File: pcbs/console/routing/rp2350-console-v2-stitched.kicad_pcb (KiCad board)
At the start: 4 copper layers, 72 x 66 mm, 81 parts, among them J1 TYPE-C-31-M-12, J2 HDMI-001S, J3 B10B-XH-A(LF)(SN), J4 B10B-XH-A(LF)(SN), J5 B2B-PH-K-S(LF)(SN), U1 SMF5.0A, U2 TLV62569DBVR, U3 RP2350B, U4 W25Q128JVSIQ, U5 PAM8302AASCR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

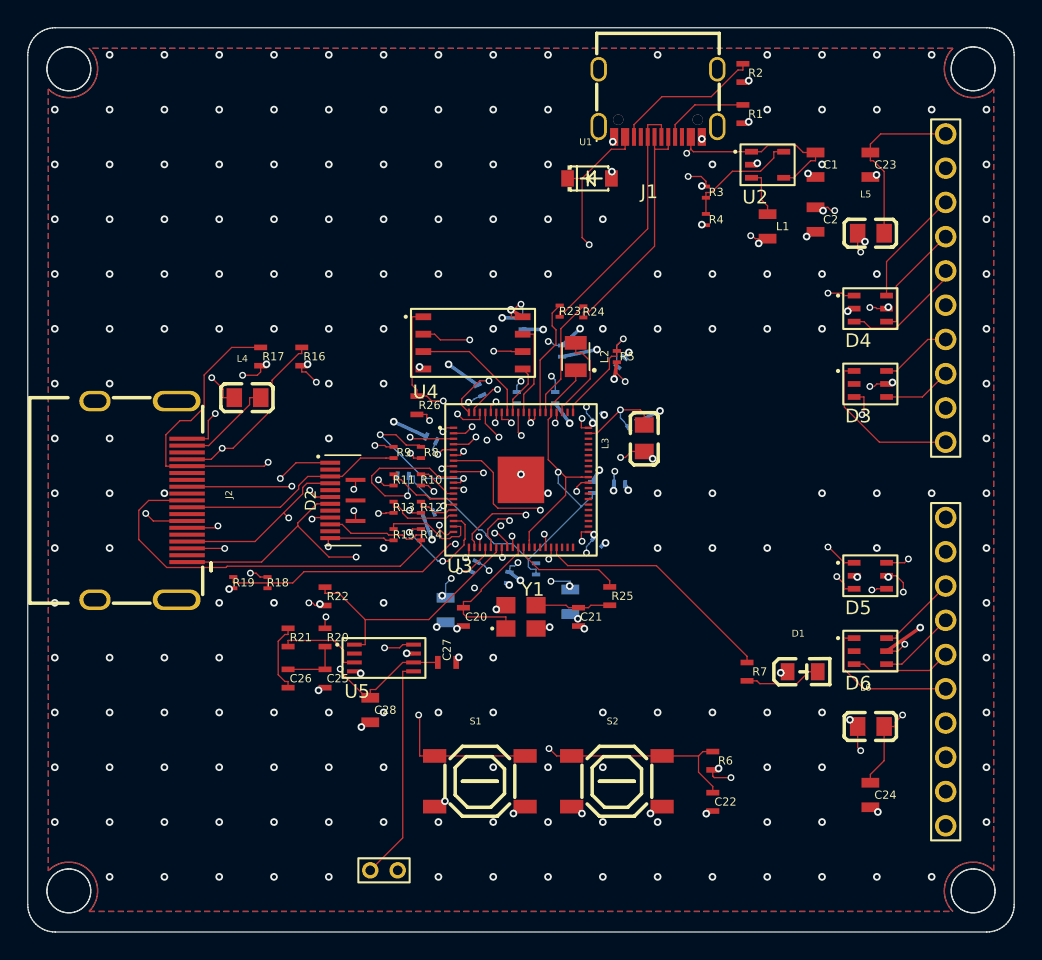
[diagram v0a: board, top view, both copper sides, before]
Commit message: feat(console): final routed board + JLCPCB fab package (v2)
GUI finishing complete (GND/V3V3 ties, V3V3 zone island, last via clearance)
on the corrected 81-part board. DRC clean: 0 unconnected, only the 2 benign
J1 USB-C shield annular (footprint-baked, allowlisted).

Fab package routing/production-v2/ (gerbers zip + drill + CPL + STEP + BOM).
BOM gated PASS: 40 grouped lines / 81 parts, all real packages + LCSC. New
parts resolved — 27R USB (C2096044), 1k (C2889391), 100nF (C1853702); SMF5.0A
as-built C2759874. The 5 DB-unindexed actives (RP2350B/USB-C/JST-XH/SRV05/AOTA)
pinned via the documented LCSC from sourcing.md.
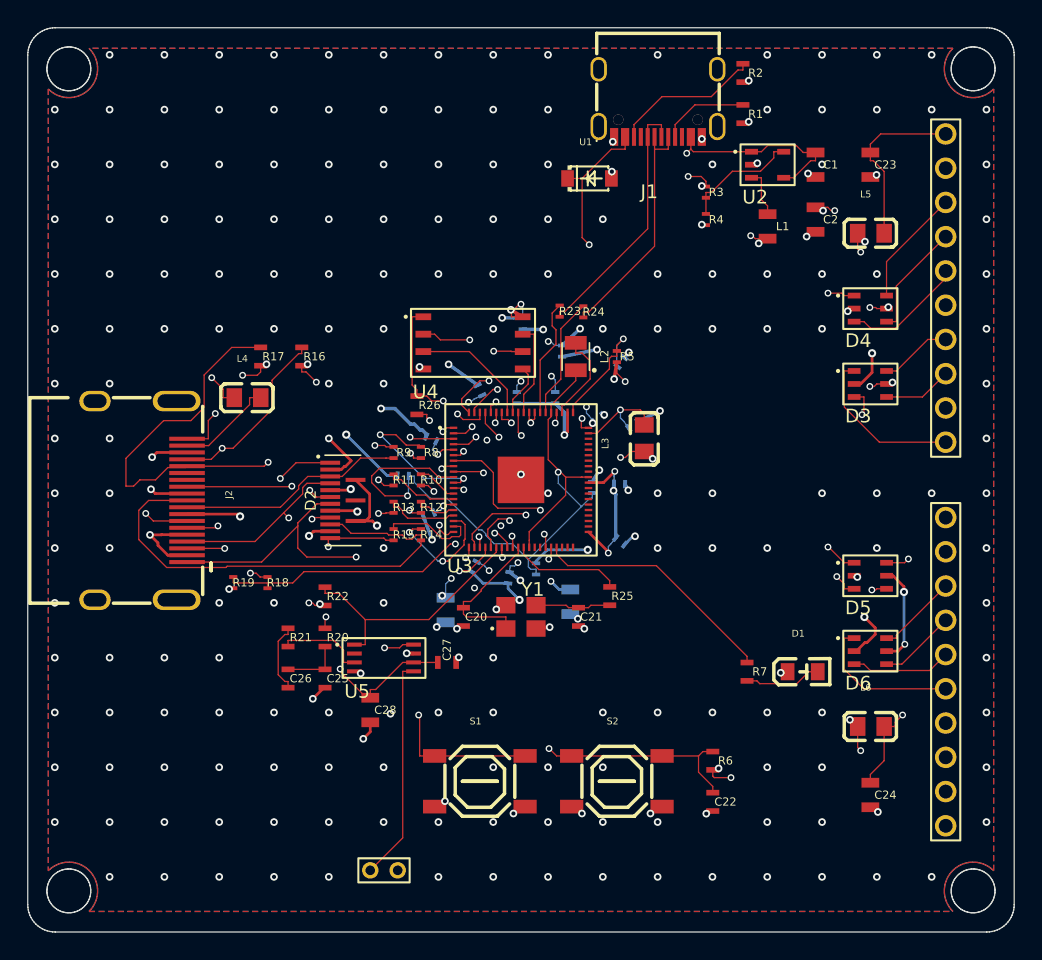
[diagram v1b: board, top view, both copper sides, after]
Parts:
- moved C10 1.59 mm to (146.7, 112.5)
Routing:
- net GND: track 18.2 -> 74.3 mm, vias 226 -> 236
- net V3V3: track 68.6 -> 78.9 mm, vias 63 -> 56
- net GPIO[27]: track 41.0 -> 47.9 mm
- net D2_P: track 23.8 -> 24.7 mm
